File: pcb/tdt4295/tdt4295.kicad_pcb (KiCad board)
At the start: 6 copper layers, 183 parts, among them J101 ARM 20 Pin Debug Header, J102 MCU USART1 Header, J103 DM1AA-SF-PEJ(21), J104 MCU GPIO Header, J301 FPGA__debug, J501 618015330923, J502 FPGA GPIO, P201 690-005-299-043, U101 EFM32GG12B810F1024GQ64, U102 COM-09032 Joystick, U103 COM-09032 Joystick, U201 PHDMI2AB4, U202 TPS54294, U203 TPS54294, U301 S25FL127SABMFV101, U302 NUP4114UCW1T2G, U303 XC7A100T-FTG256-tdt4295, U501 NUP4114UCW1T2G, U502 NUP4114UCW1T2G, U503 NUP4114UCW1T2G, U504 NUP4114UCW1T2G, U601 DSC1001AL5-100.0000, Y101 48MHz

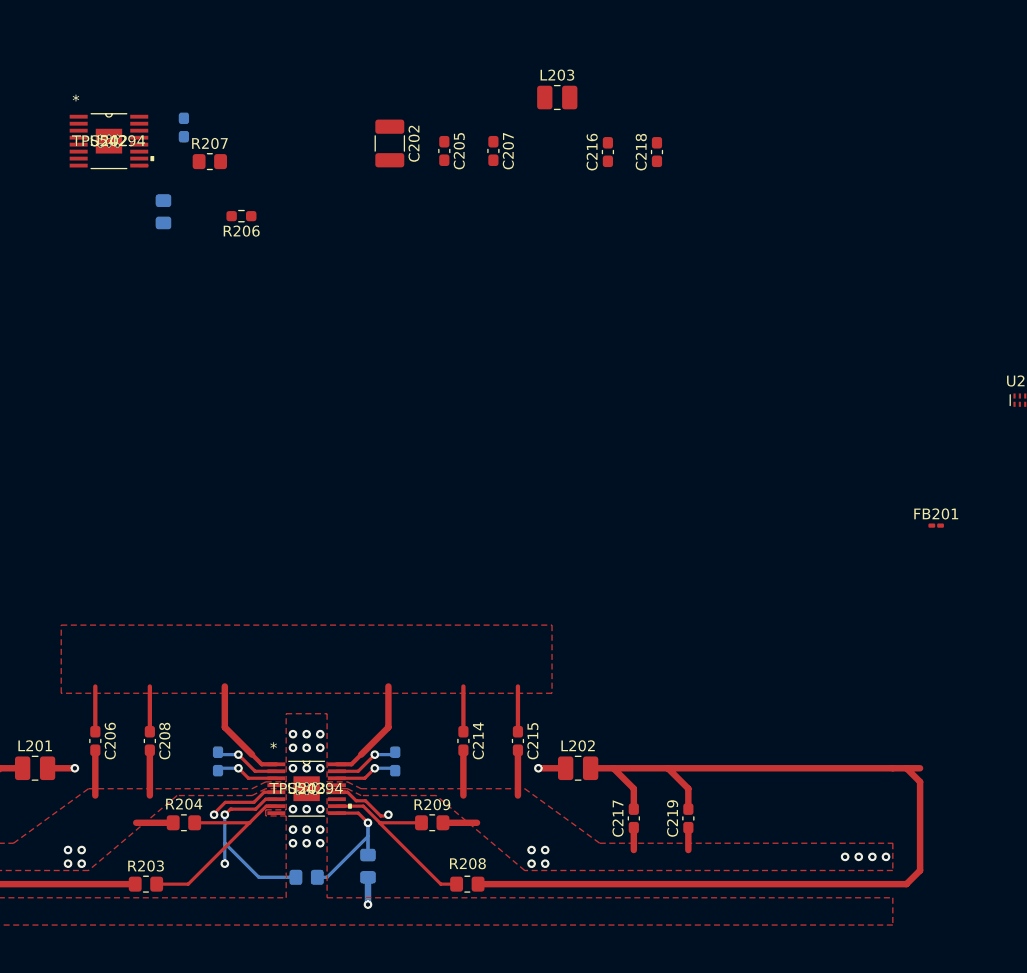
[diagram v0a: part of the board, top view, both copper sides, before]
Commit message: minor routing changes
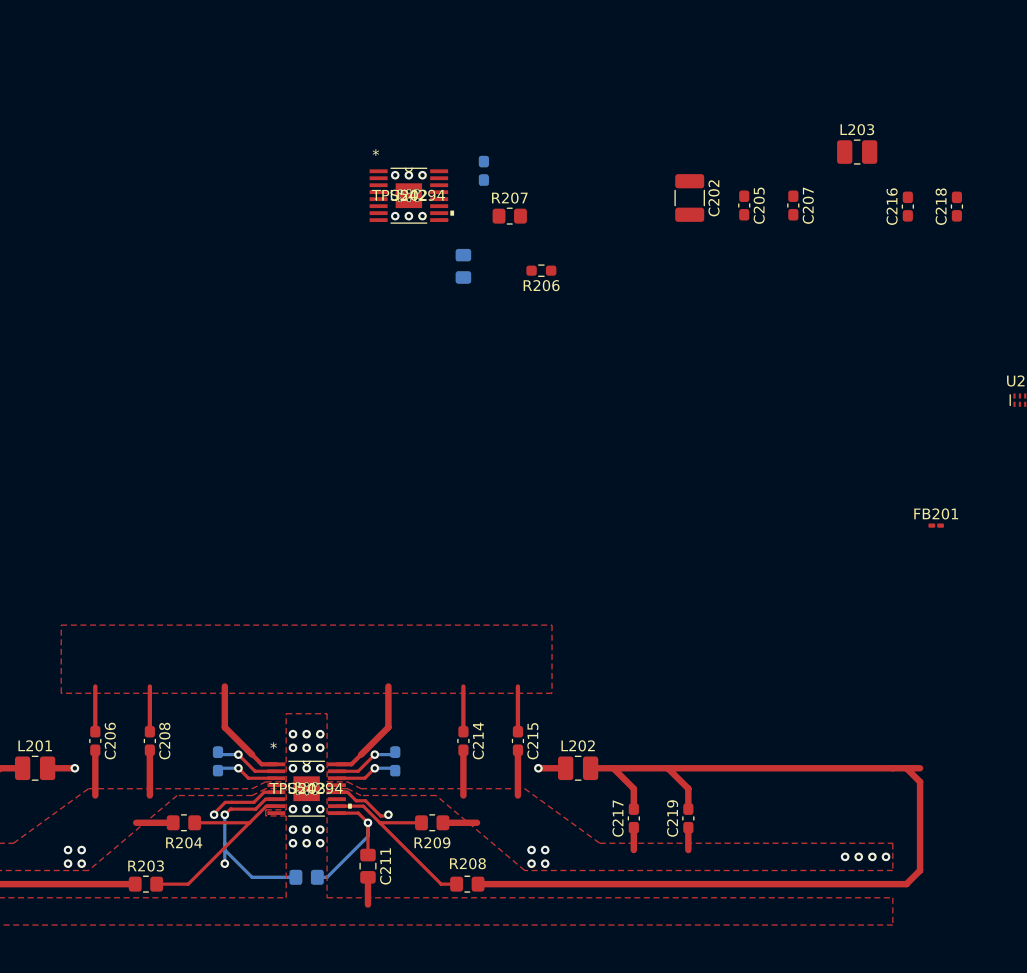
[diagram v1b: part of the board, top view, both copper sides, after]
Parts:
- C211: moved to F.Cu
- moved C207 28.4 mm to (274.6, 50.4)
- moved C202 28.4 mm to (264.9, 49.7)
- moved L203 28.4 mm to (280.5, 45.5)
- moved C205 28.4 mm to (270.0, 50.4)
- moved R207 28.4 mm to (248.2, 51.4)
- moved C210 28.4 mm to (243.8, 56.1)
- moved C216 28.4 mm to (285.2, 50.5)
- moved C218 28.4 mm to (289.8, 50.5)
- moved R206 28.4 mm to (251.1, 56.5)
- moved U202 28.4 mm to (238.8, 49.5)
- moved C213 28.2 mm to (245.7, 47.2)
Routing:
- net GND: track 72.7 -> 65.3 mm, vias 75 -> 80
- net Net-(C211-Pad1): track 12.6 -> 13.8 mm
- net Net-(R205-Pad2): track 42.4 -> 42.9 mm

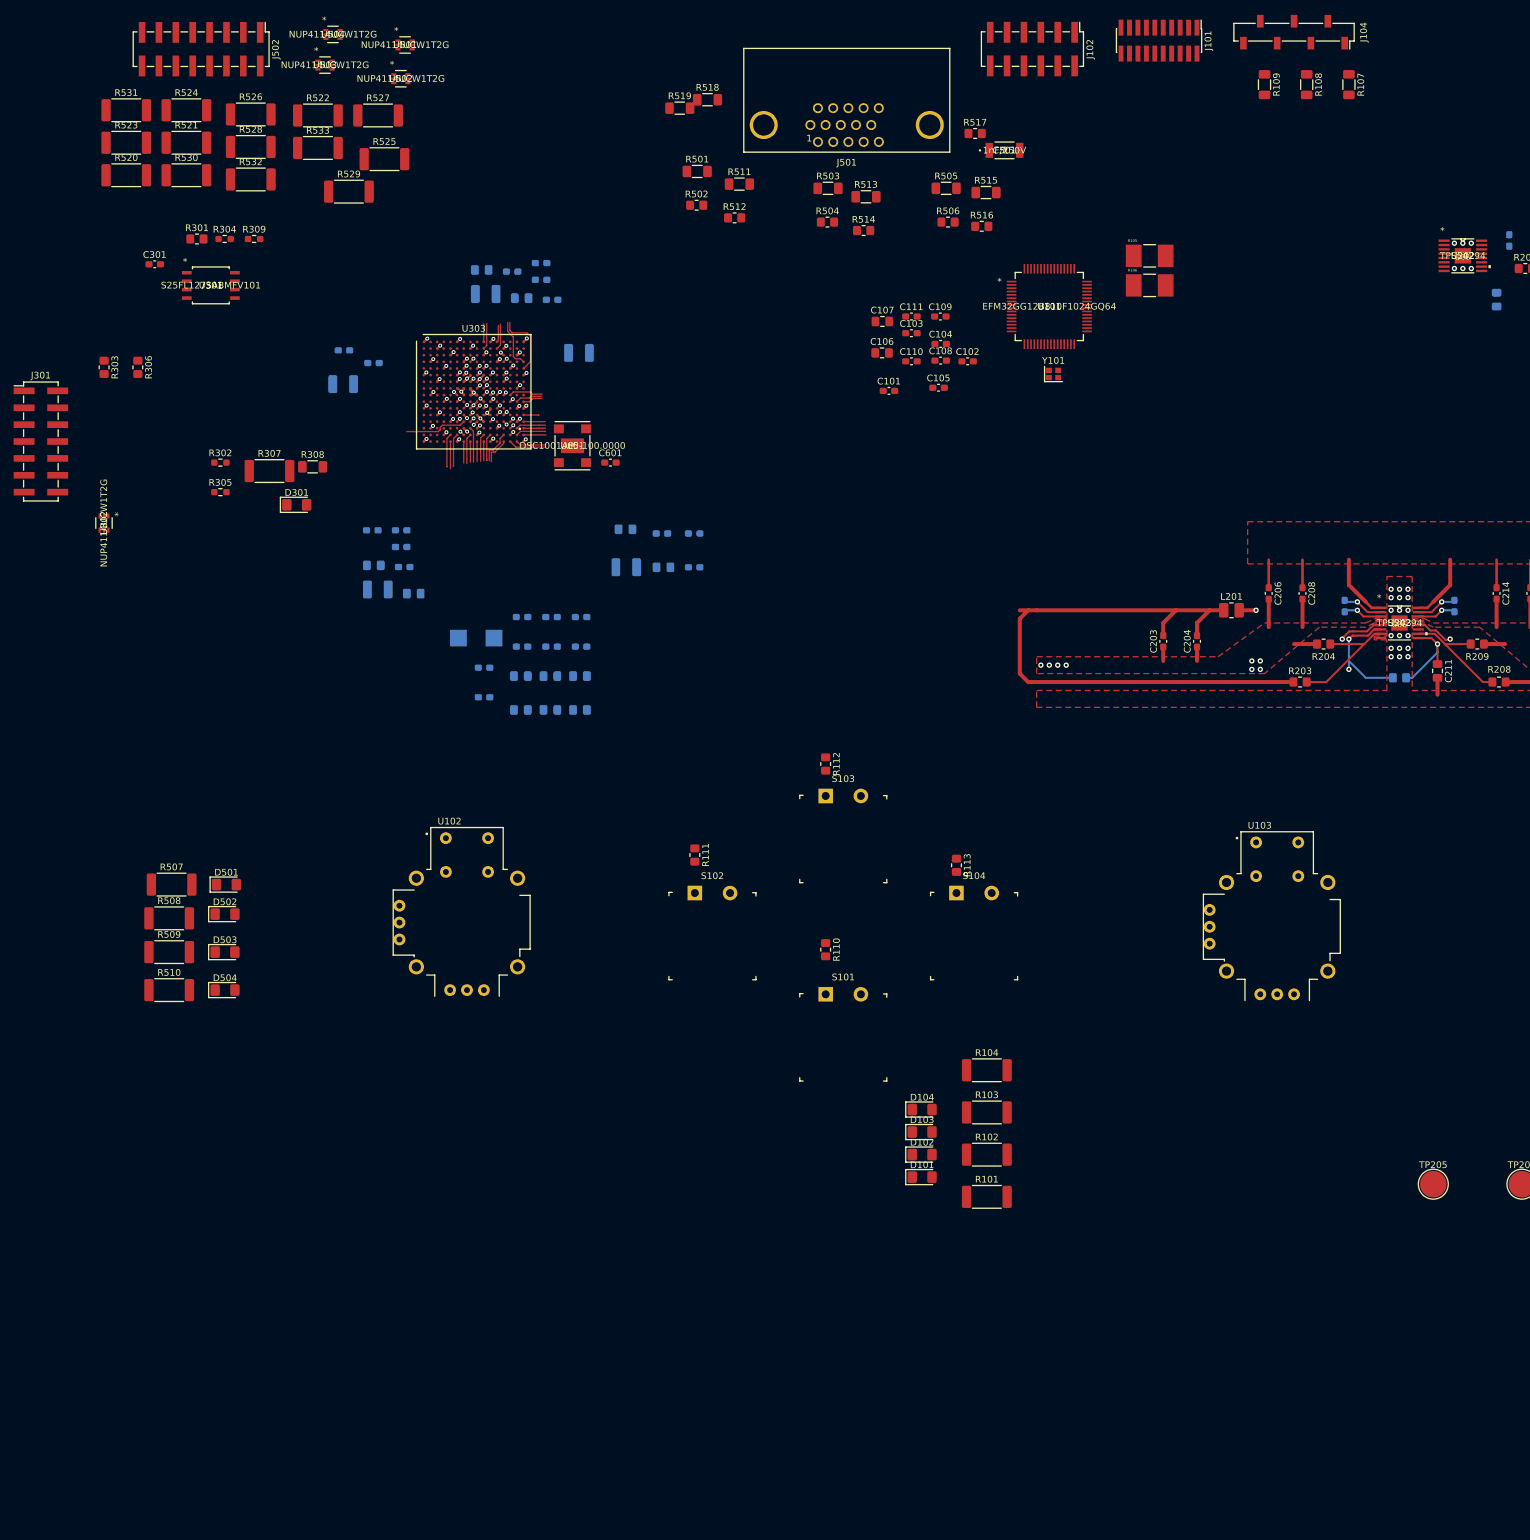
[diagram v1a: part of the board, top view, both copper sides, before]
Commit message: placing out components, more routing from FPGA
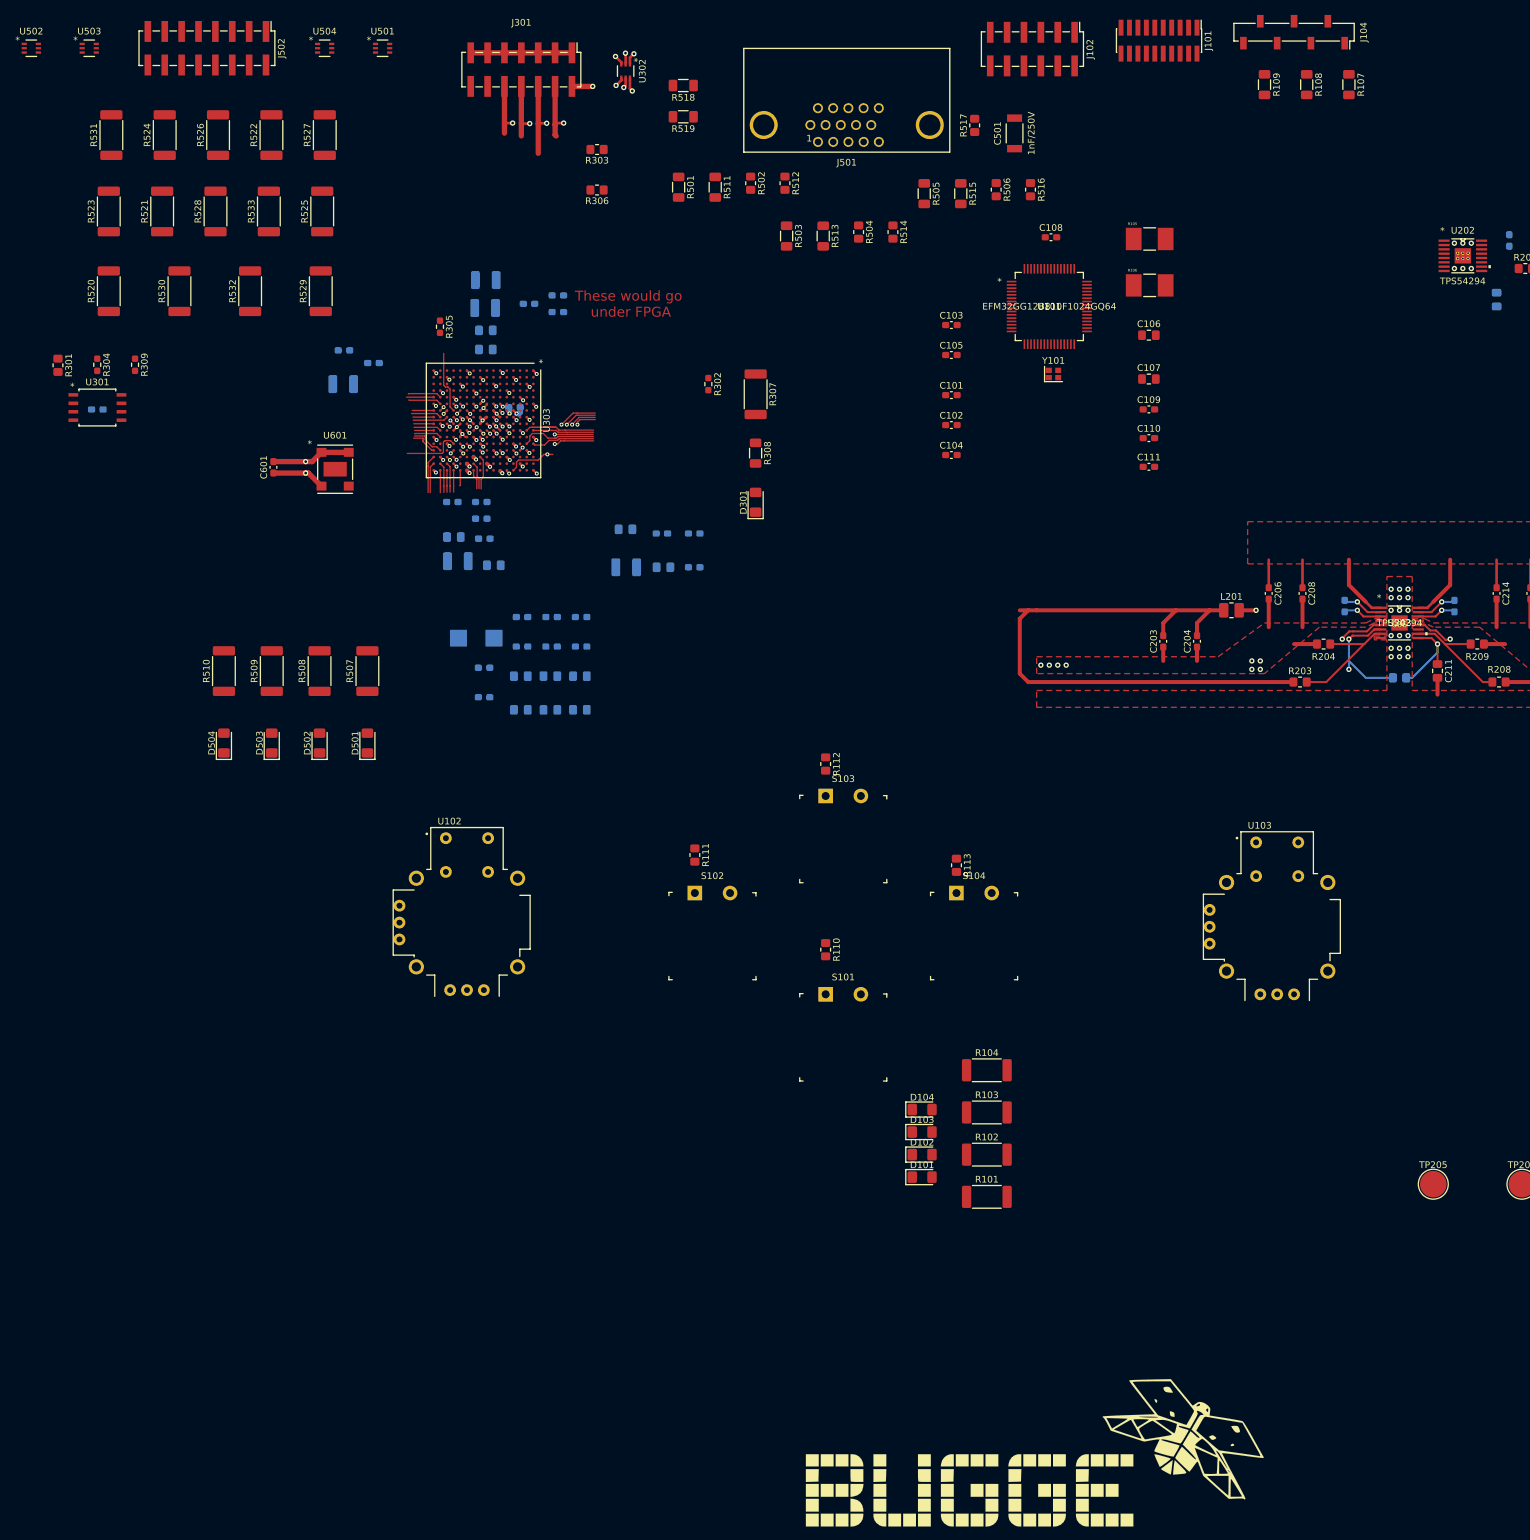
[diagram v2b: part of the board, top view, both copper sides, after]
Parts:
- added G***: LOGO, Graphics:buggelogo_inverted, F.Cu at (174.2, 229.9)
- C301: moved to B.Cu
- U302, U501, U502, U503, U504: value NUP4114UCW1T2G -> SOIC_W1T2G_ONS
- moved U302 103.9 mm to (112.8, 21.7)
- moved J301 91.4 mm to (97.1, 21.5), turned to 270 degrees
- moved R303 81.1 mm to (108.5, 33.5), turned to 180 degrees
- moved R302 74.4 mm to (125.2, 68.8), turned to 270 degrees
- moved R306 74.1 mm to (108.5, 39.6), turned to 180 degrees
- moved R307 74.1 mm to (132.3, 70.4), turned to 270 degrees
- moved D301 69.1 mm to (132.3, 86.6), turned to 90 degrees
- moved R308 66.7 mm to (132.3, 79.2), turned to 270 degrees
- moved U502 55.8 mm to (23.3, 18.3)
- moved C601 50.7 mm to (59.8, 81.3), turned to 90 degrees
- moved R510 48.7 mm to (52.3, 112.0), turned to 90 degrees
- moved R509 45.0 mm to (59.5, 112.0), turned to 90 degrees
- moved R507 43.6 mm to (73.9, 112.0), turned to 90 degrees
- moved R508 43.6 mm to (66.7, 112.0), turned to 90 degrees
- moved C111 42.3 mm to (191.5, 81.3)
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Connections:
- J101 pad 11: Net-(J101-Pad11) -> (no net)
- J101 pad 17: Net-(J101-Pad17) -> (no net)
- J101 pad 19: Net-(J101-Pad19) -> (no net)
- J101 pad 2: Net-(J101-Pad2) -> (no net)
- J101 pad 3: Net-(J101-Pad3) -> (no net)
- J101 pad 5: Net-(J101-Pad5) -> (no net)
- J103 pad 12: Net-(J103-Pad12) -> (no net)
- J103 pad 13: Net-(J103-Pad13) -> (no net)
- J104 pad 5: Net-(J104-Pad5) -> (no net)
- J104 pad 6: Net-(J104-Pad6) -> (no net)
- J301 pad 12: Net-(J301-Pad12) -> (no net)
- J301 pad 14: Net-(J301-Pad14) -> (no net)
- J501 pad 11: Net-(J501-Pad11) -> (no net)
- J501 pad 12: Net-(J501-Pad12) -> (no net)
- J501 pad 15: Net-(J501-Pad15) -> (no net)
- J501 pad 4: Net-(J501-Pad4) -> (no net)
- J501 pad 9: Net-(J501-Pad9) -> (no net)
- P201 pad 4: Net-(P201-Pad4) -> (no net)
- U101 pad 37: Net-(U101-Pad37) -> (no net)
- U101 pad 45: Net-(U101-Pad45) -> (no net)
- U102 pad B1A: Net-(U102-PadB1A) -> (no net)
- U102 pad B2A: Net-(U102-PadB2A) -> (no net)
- U103 pad B1A: Net-(U103-PadB1A) -> (no net)
- U103 pad B2A: Net-(U103-PadB2A) -> (no net)
- U201 pad 10: Net-(U201-Pad10) -> (no net)
- U201 pad 5: Net-(U201-Pad5) -> (no net)
- U201 pad 6: Net-(U201-Pad6) -> (no net)
- U201 pad 7: Net-(U201-Pad7) -> (no net)
- U201 pad 9: Net-(U201-Pad9) -> (no net)
- U202 pad 2: Net-(U202-Pad2) -> (no net)
- U202 pad 3: Net-(U202-Pad3) -> (no net)
- U202 pad 6: Net-(U202-Pad6) -> (no net)
- U202 pad 7: Net-(U202-Pad7) -> (no net)
- U203 pad 11: Net-(U203-Pad11) -> (no net)
- U203 pad V: GND -> (no net)
- U303 pad A13: Net-(U303-PadA13) -> (no net)
- U303 pad A14: Net-(U303-PadA14) -> (no net)
- U303 pad A15: Net-(U303-PadA15) -> (no net)
- U303 pad A8: Net-(U303-PadA8) -> (no net)
- U303 pad A9: Net-(U303-PadA9) -> (no net)
- U303 pad B11: Net-(U303-PadB11) -> (no net)
- U303 pad B14: Net-(U303-PadB14) -> (no net)
- U303 pad B15: Net-(U303-PadB15) -> (no net)
- U303 pad B16: Net-(U303-PadB16) -> (no net)
- U303 pad B9: Net-(U303-PadB9) -> (no net)
- U303 pad C11: Net-(U303-PadC11) -> (no net)
- U303 pad C12: Net-(U303-PadC12) -> (no net)
- U303 pad C14: Net-(U303-PadC14) -> (no net)
- U303 pad C16: Net-(U303-PadC16) -> (no net)
- U303 pad C8: Net-(U303-PadC8) -> (no net)
- U303 pad C9: Net-(U303-PadC9) -> (no net)
- U303 pad D10: Net-(U303-PadD10) -> (no net)
- U303 pad D11: Net-(U303-PadD11) -> (no net)
- U303 pad D14: Net-(U303-PadD14) -> (no net)
- U303 pad D15: Net-(U303-PadD15) -> (no net)
- U303 pad D9: Net-(U303-PadD9) -> (no net)
- U303 pad E11: Net-(U303-PadE11) -> (no net)
- U303 pad E12: Net-(U303-PadE12) -> (no net)
- U303 pad E13: Net-(U303-PadE13) -> (no net)
- U303 pad E15: Net-(U303-PadE15) -> (no net)
- U303 pad F12: Net-(U303-PadF12) -> (no net)
- U303 pad F14: Net-(U303-PadF14) -> (no net)
- U303 pad F15: Net-(U303-PadF15) -> (no net)
- U303 pad G11: Net-(U303-PadG11) -> (no net)
- U303 pad G12: Net-(U303-PadG12) -> (no net)
- U303 pad G14: Net-(U303-PadG14) -> (no net)
- U303 pad G15: Net-(U303-PadG15) -> (no net)
- U303 pad G16: Net-(U303-PadG16) -> (no net)
- U303 pad H11: Net-(U303-PadH11) -> (no net)
- U303 pad H12: Net-(U303-PadH12) -> (no net)
- U303 pad H13: Net-(U303-PadH13) -> (no net)
- U303 pad H14: Net-(U303-PadH14) -> (no net)
- U303 pad H16: Net-(U303-PadH16) -> (no net)
- U303 pad J15: Net-(U303-PadJ15) -> (no net)
- U303 pad J16: Net-(U303-PadJ16) -> (no net)
- U303 pad K12: Net-(U303-PadK12) -> (no net)
- U303 pad K13: Net-(U303-PadK13) -> (no net)
- U303 pad K7: Net-(U303-PadK7) -> (no net)
- U303 pad K8: Net-(U303-PadK8) -> (no net)
- U303 pad L13: Net-(U303-PadL13) -> (no net)
- U303 pad L14: Net-(U303-PadL14) -> (no net)
- U303 pad M14: Net-(U303-PadM14) -> (no net)
- U303 pad M15: Net-(U303-PadM15) -> (no net)
- U303 pad P10: Net-(U303-PadP10) -> (no net)
- U303 pad P11: Net-(U303-PadP11) -> (no net)
- U303 pad P6: Net-(U303-PadP6) -> (no net)
- U303 pad R12: Net-(U303-PadR12) -> (no net)
- U303 pad T12: Net-(U303-PadT12) -> (no net)
- U501 pad 4: Net-(U501-Pad4) -> (no net)
- U504 pad 4: Net-(U504-Pad4) -> (no net)
- U601 pad 5: Net-(U601-Pad5) -> (no net)
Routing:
- net /FPGA/TDO_JTAG: track 11.4 -> 44.0 mm, vias 1 -> 3
- net /FPGA/TDI_JTAG: track 9.42 -> 41.6 mm, vias 0 -> 2
- net /FPGA/TCK_JTAG: track 16.2 -> 43.1 mm, vias 1 -> 3
- net GND: track 65.3 -> 91.7 mm, vias 80 -> 82
- net /FPGA/TMS_JTAG: track 10.0 -> 33.4 mm, vias 1 -> 3
- net +3V3: track 100.7 -> 118.3 mm, vias 13 -> 16
- net FPGA_MCU_GPIO_0: track 5.02 -> 17.1 mm, vias 1 -> 2
- net FPGA_MCU_USART_RX: track 3.98 -> 15.1 mm
- net FPGA_MCU_GPIO_1: track 8.11 -> 19.0 mm, vias 1 -> 2
- net FPGA_MCU_GPIO_3: track 7.38 -> 18.1 mm, vias 0 -> 2
- net FPGA_MCU_GPIO_2: track 9.94 -> 20.3 mm, vias 0 -> 2
- net /FPGA/IOB14/GCLK100: track 0.00 -> 8.86 mm
- net FPGA_MCU_USART_CLK: track 6.63 -> 14.3 mm, vias 1 -> 2
- net FPGA_MCU_USART_CS: track 3.90 -> 11.5 mm
- net FPGA_MCU_USART_CTS: track 6.87 -> 14.2 mm, vias 1 -> 2
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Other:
- board text added: "These would go under FPGA"
